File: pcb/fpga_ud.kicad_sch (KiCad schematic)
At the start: 1 part

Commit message: kicad said I needed to save
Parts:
- U?: value (none) -> XC7A100T-FTG256
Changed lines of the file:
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@@
     (in_bom yes) (on_board yes) (fields_autoplaced)
     (property "Reference" "U?" (id 0) (at 96.52 44.45 0))
-    (property "Value" "" (id 1) (at 96.52 46.99 0))
+    (property "Value" "XC7A100T-FTG256" (id 1) (at 96.52 46.99 0))
     (property "Footprint" "" (id 2) (at 96.52 85.09 0)
       (effects (font (size 1.27 1.27)) hide)

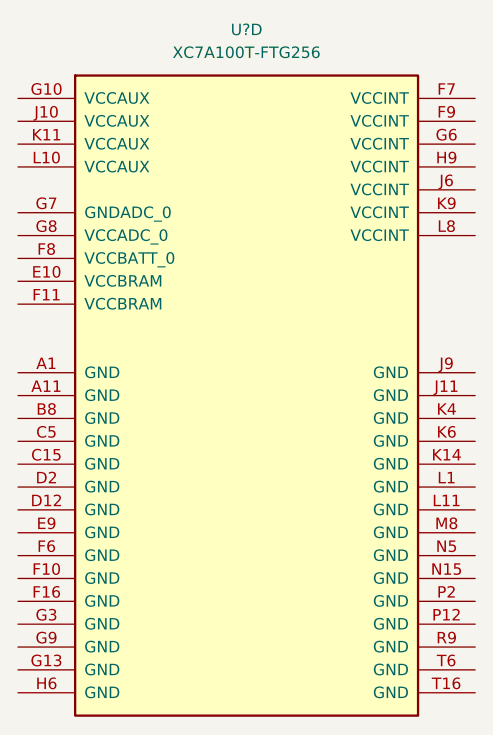
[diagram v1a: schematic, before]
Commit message: add flash memory component for fpga
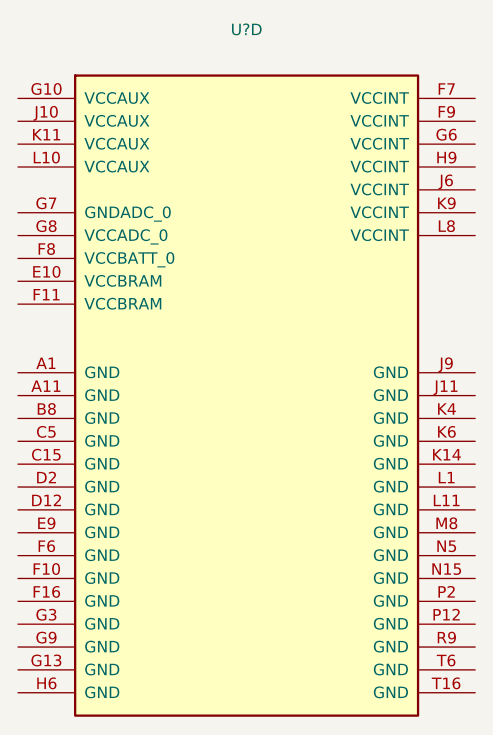
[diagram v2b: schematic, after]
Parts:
- U?: value XC7A100T-FTG256 -> (none)
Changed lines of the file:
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@@
     (in_bom yes) (on_board yes) (fields_autoplaced)
     (property "Reference" "U?" (id 0) (at 96.52 44.45 0))
-    (property "Value" "XC7A100T-FTG256" (id 1) (at 96.52 46.99 0))
+    (property "Value" "" (id 1) (at 96.52 46.99 0))
     (property "Footprint" "" (id 2) (at 96.52 85.09 0)
       (effects (font (size 1.27 1.27)) hide)
